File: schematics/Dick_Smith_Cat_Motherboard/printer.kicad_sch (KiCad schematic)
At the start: 5 parts, among them J3 Printer, U33 74LS373

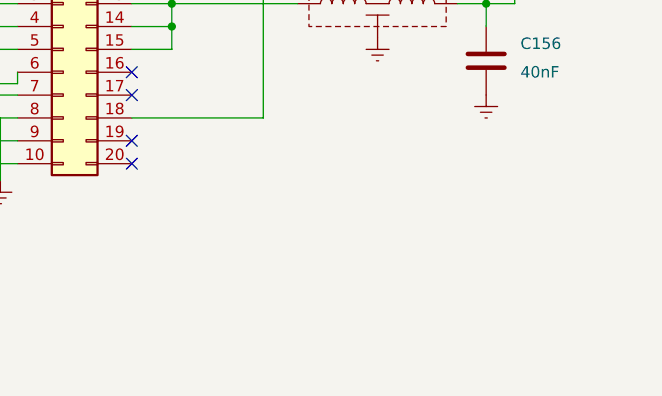
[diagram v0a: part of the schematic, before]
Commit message: Add more connector pinouts to the schematics
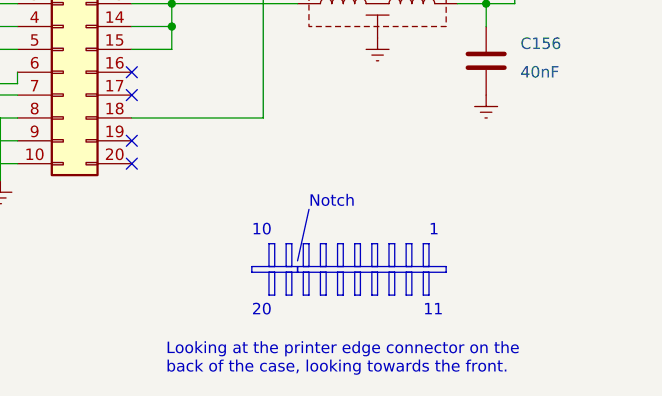
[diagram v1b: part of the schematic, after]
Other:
- note added: "1"
- note added: "10"
- note added: "11"
- note added: "20"
- note added: "Looking at the printer edge connector on the back of the case, looking towards the front."
- note added: "Notch"
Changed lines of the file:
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@@
+    (stroke (width 0) (type default))
+  )
+  (polyline (pts (xy 172.085 97.155) (xy 170.815 102.87))
     (stroke (width 0) (type default))
   )
@@
     (stroke (width 0) (type default))
   )
+  (rectangle (start 170.815 103.505) (end 187.325 104.14)
+    (stroke (width 0) (type default))
+    (fill (type none))
+  )
+  (rectangle (start 184.785 104.14) (end 185.42 106.68)
+    (stroke (width 0) (type default))
+    (fill (type none))
+  )
+  (rectangle (start 175.26 100.965) (end 175.895 103.505)
+    (stroke (width 0) (type default))
+    (fill (type none))
+  )
+  (rectangle (start 167.64 100.965) (end 168.275 103.505)
+    (stroke (width 0) (type default))
+    (fill (type none))
+  )
+  (rectangle (start 180.975 104.14) (end 181.61 106.68)
+    (stroke (width 0) (type default))
+    (fill (type none))
+  )
+  (rectangle (start 179.07 104.14) (end 179.705 106.68)
+    (stroke (width 0) (type default))
+    (fill (type none))
+  )
+  (rectangle (start 173.355 100.965) (end 173.99 103.505)
+    (stroke (width 0) (type default))
+    (fill (type none))
+  )
+  (rectangle (start 167.64 104.14) (end 168.275 106.68)
+    (stroke (width 0) (type default))
+    (fill (type none))
+  )
+  (rectangle (start 179.07 100.965) (end 179.705 103.505)
+    (stroke (width 0) (type default))
+    (fill (type none))
+  )
+  (rectangle (start 184.785 100.965) (end 185.42 103.505)
+    (stroke (width 0) (type default))
+    (fill (type none))
+  )
+  (rectangle (start 177.165 104.14) (end 177.8 106.68)
+    (stroke (width 0) (type default))
+    (fill (type none))
+  )
+  (rectangle (start 171.45 100.965) (end 172.085 103.505)
+    (stroke (width 0) (type default))
+    (fill (type none))
+  )
+  (rectangle (start 169.545 100.965) (end 170.18 103.505)
+    (stroke (width 0) (type default))
+    (fill (type none))
+  )
+  (rectangle (start 182.88 100.965) (end 183.515 103.505)
+    (stroke (width 0) (type default))
+    (fill (type none))
+  )
+  (rectangle (start 180.975 100.965) (end 181.61 103.505)
+    (stroke (width 0) (type default))
+    (fill (type none))
+  )
+  (rectangle (start 182.88 104.14) (end 183.515 106.68)
+    (stroke (width 0) (type default))
+    (fill (type none))
+  )
+  (rectangle (start 173.355 104.14) (end 173.99 106.68)
+    (stroke (width 0) (type default))
+    (fill (type none))
+  )
+  (rectangle (start 171.45 104.14) (end 172.085 106.68)
+    (stroke (width 0) (type default))
+    (fill (type none))
+  )
+  (rectangle (start 169.545 104.14) (end 170.18 106.68)
+    (stroke (width 0) (type default))
+    (fill (type none))
+  )
+  (rectangle (start 175.26 104.14) (end 175.895 106.68)
+    (stroke (width 0) (type default))
+    (fill (type none))
+  )
+  (rectangle (start 165.735 103.505) (end 170.815 104.14)
+    (stroke (width 0) (type default))
+    (fill (type none))
+  )
+  (rectangle (start 177.165 100.965) (end 177.8 103.505)
+    (stroke (width 0) (type default))
+    (fill (type none))
+  )
+  (text "20" (at 165.735 109.22 0)
+    (effects (font (size 1.27 1.27)) (justify left bottom))
+  )
+  (text "10" (at 165.735 100.33 0)
+    (effects (font (size 1.27 1.27)) (justify left bottom))
+  )
+  (text "Notch" (at 172.085 97.155 0)
+    (effects (font (size 1.27 1.27)) (justify left bottom))
+  )
+  (text "1" (at 185.42 100.33 0)
+    (effects (font (size 1.27 1.27)) (justify left bottom))
+  )
+  (text "Looking at the printer edge connector on the\nback of the case, looking towards the front."
+    (at 156.21 115.57 0)
+    (effects (font (size 1.27 1.27)) (justify left bottom))
+  )
+  (text "11" (at 184.785 109.22 0)
+    (effects (font (size 1.27 1.27)) (justify left bottom))
+  )
   (label "BD7" (at 90.805 89.535 180) (fields_autoplaced)
